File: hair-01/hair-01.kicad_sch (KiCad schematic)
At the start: 37 parts, among them J1 TYPE-C-31-M-12, Q1 BC847, Q2 BC847, Q3 2N7002, U1 ESP-12F, U2 AP2112K-3.3, U3 CP2102N-Axx-xQFN24, U4 TSMP58000

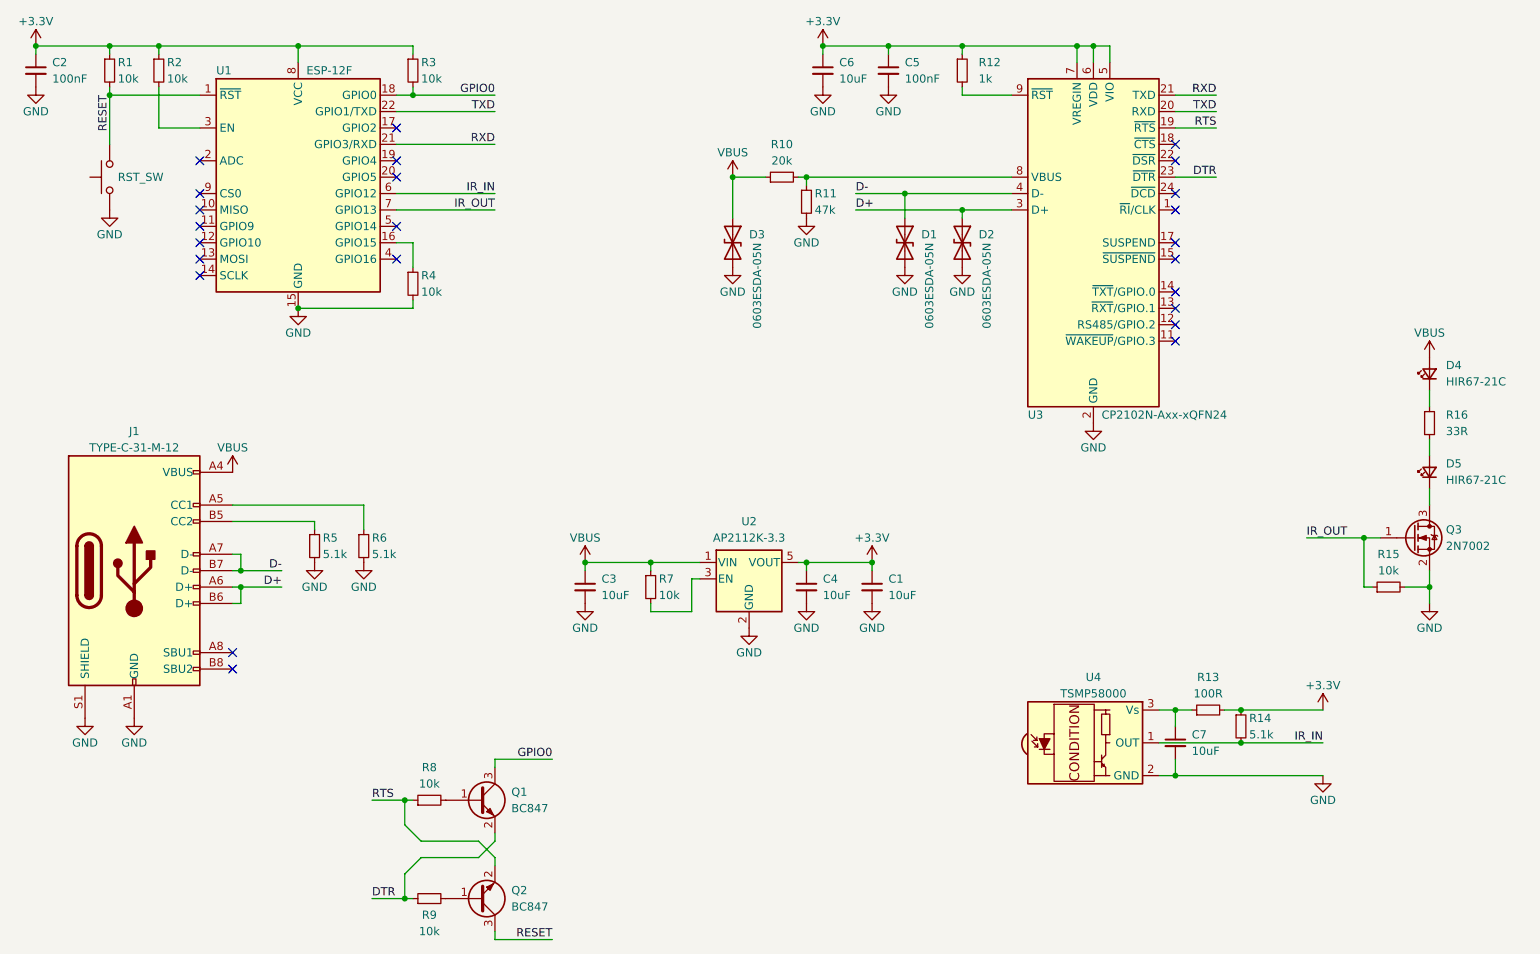
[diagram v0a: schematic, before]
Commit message: hair-01: Add footprints and start board layout
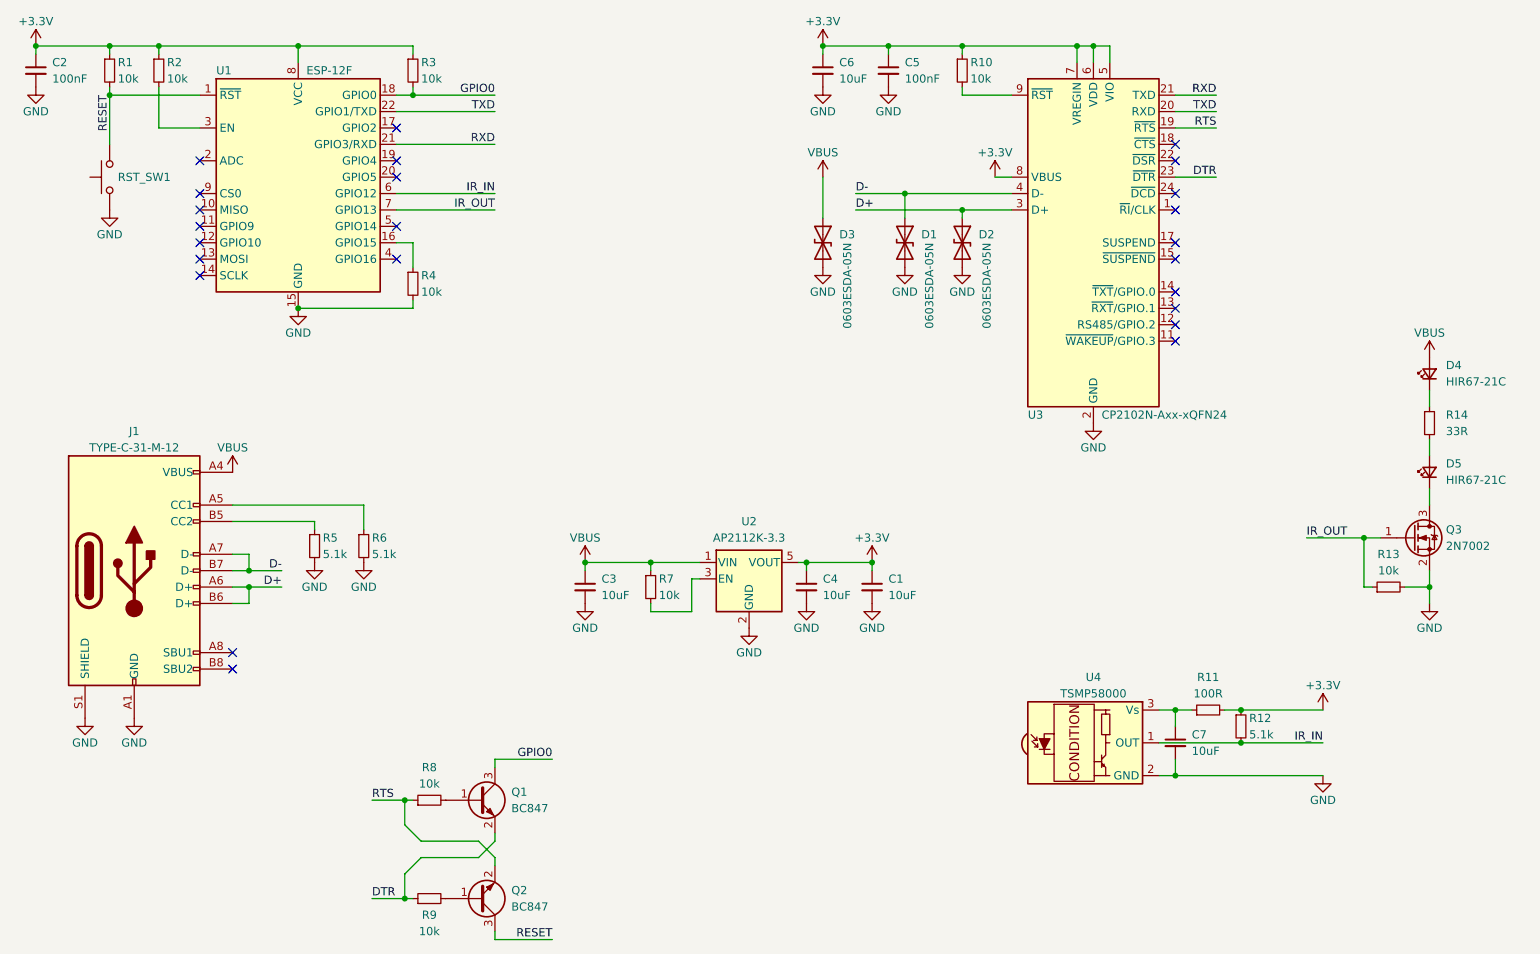
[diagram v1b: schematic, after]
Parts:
- removed R11: 47k, Resistor_SMD:R_0603_1608Metric, symbol Device:R_Small
- removed R12: 1k, Resistor_SMD:R_0603_1608Metric, symbol Device:R_Small
- D4, D5: footprint LED_SMD:LED_1210_3225Metric_Pad1.42x2.65mm_HandSolder -> hair-01:LED_Everlight_HIR67-21C
- R10: value 20k -> 10k; LCSC C4184 -> C25804
- U4: footprint OptoDevice:Vishay_MINICAST-3Pin -> hair-01:Vishay_MINICAST-3Pin-SMD
- renumbered R13 to R11, R14 to R12, R15 to R13, R16 to R14, RST_SW to RST_SW1
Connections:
- net +3V3: now also R10.1, U3.8 (VBUS)
- net VBUS: no longer R10.1
- net at R10.2: now also U3.9 (~{RST}); no longer U3.8 (VBUS)
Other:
- moved on the sheet: D3

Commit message: hair-01: Replace reset button and more routing
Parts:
- RST_SW1: footprint Button_Switch_SMD:SW_Push_1P1T-MP_NO_Horizontal_Alps_SKRTLAE010 -> Button_Switch_SMD:SW_Push_SPST_NO_Alps_SKRK; LCSC C110293 -> C202388
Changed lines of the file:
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@@
       (effects (font (size 1.27 1.27)) (justify right) hide)
     )
-    (property "Footprint" "Button_Switch_SMD:SW_Push_1P1T-MP_NO_Horizontal_Alps_SKRTLAE010" (id 2) (at 41.91 58.42 0)
+    (property "Footprint" "Button_Switch_SMD:SW_Push_SPST_NO_Alps_SKRK" (id 2) (at 41.91 58.42 0)
       (effects (font (size 1.27 1.27)) hide)
     )
@@
       (effects (font (size 1.27 1.27)) hide)
     )
-    (property "LCSC" "C110293" (id 4) (at 46.99 58.42 90)
+    (property "LCSC" "C202388" (id 4) (at 46.99 58.42 90)
       (effects (font (size 1.27 1.27)) hide)
     )
@@
     )
     (path "/74adff30-1759-49f6-8036-03af26649b8b"
-      (reference "RST_SW1") (unit 1) (value "SW_Push") (footprint "Button_Switch_SMD:SW_Push_1P1T-MP_NO_Horizontal_Alps_SKRTLAE010")
+      (reference "RST_SW1") (unit 1) (value "SW_Push") (footprint "Button_Switch_SMD:SW_Push_SPST_NO_Alps_SKRK")
     )
     (path "/5778953d-c3f1-4eab-88e0-47485d04ab27"
